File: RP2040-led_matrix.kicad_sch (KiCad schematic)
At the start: 27 parts, among them J2 USB_C_Receptacle, SW2 SW_DIP_x01, U1 W25Q16JVSS, U2 RP2040, U4 NCP1117-1.5_SOT223, Y2 ABM8-272-T3

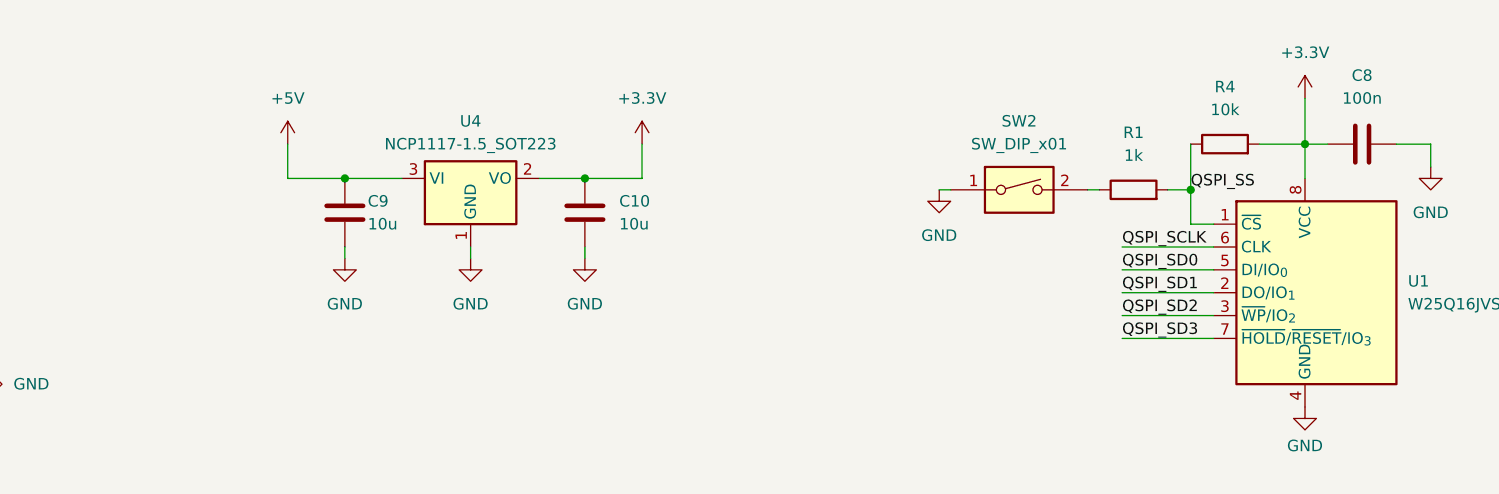
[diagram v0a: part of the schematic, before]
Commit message: Modified power supply stage
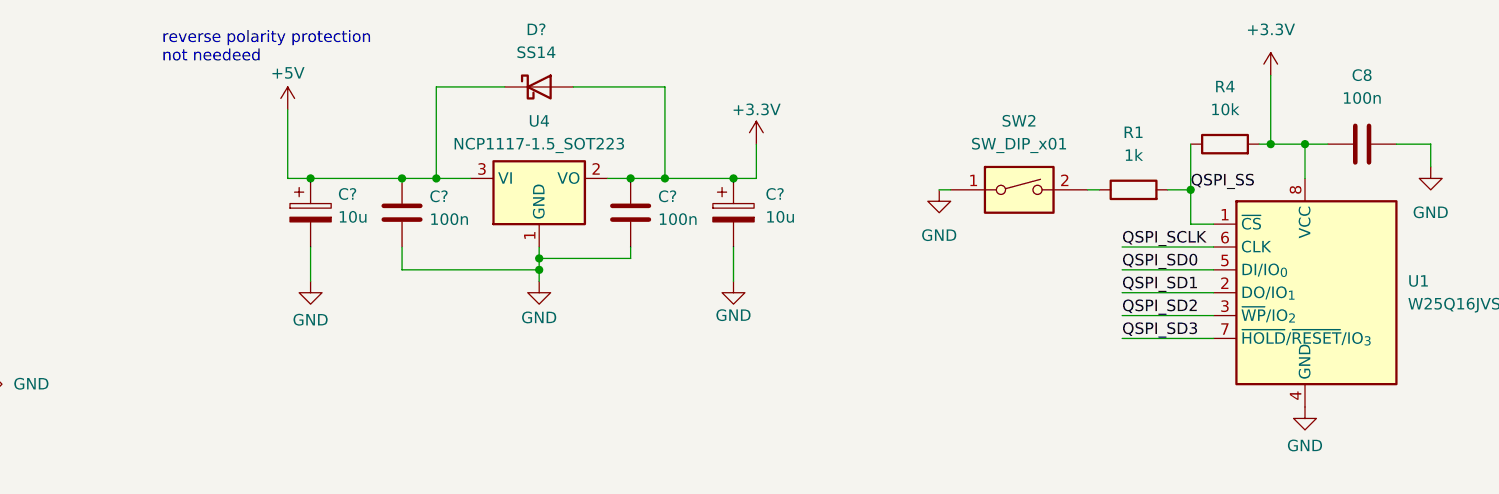
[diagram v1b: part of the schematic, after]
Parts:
- removed C10, C9: 10u, Capacitor_SMD:C_0603_1608Metric, symbol Device:C
- added C? (x2): 10u, Capacitor_SMD:CP_Elec_5x5.4, symbol Device:C_Polarized
- added C? (x2): 100n, Capacitor_SMD:C_0805_2012Metric, symbol Device:C
- added D?: SS14, Diode_THT:D_DO-41_SOD81_P10.16mm_Horizontal, symbol Diode:SS14
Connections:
- net +3.3V: now also C?.1, C?.1, D?.2 (A)
- net +5V: now also C?.1, C?.1, D?.1 (K)
- net GND: now also C?.2, C?.2, C?.2, C?.2
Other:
- note added: "reverse polarity protection not needeed"
- moved on the sheet: U4

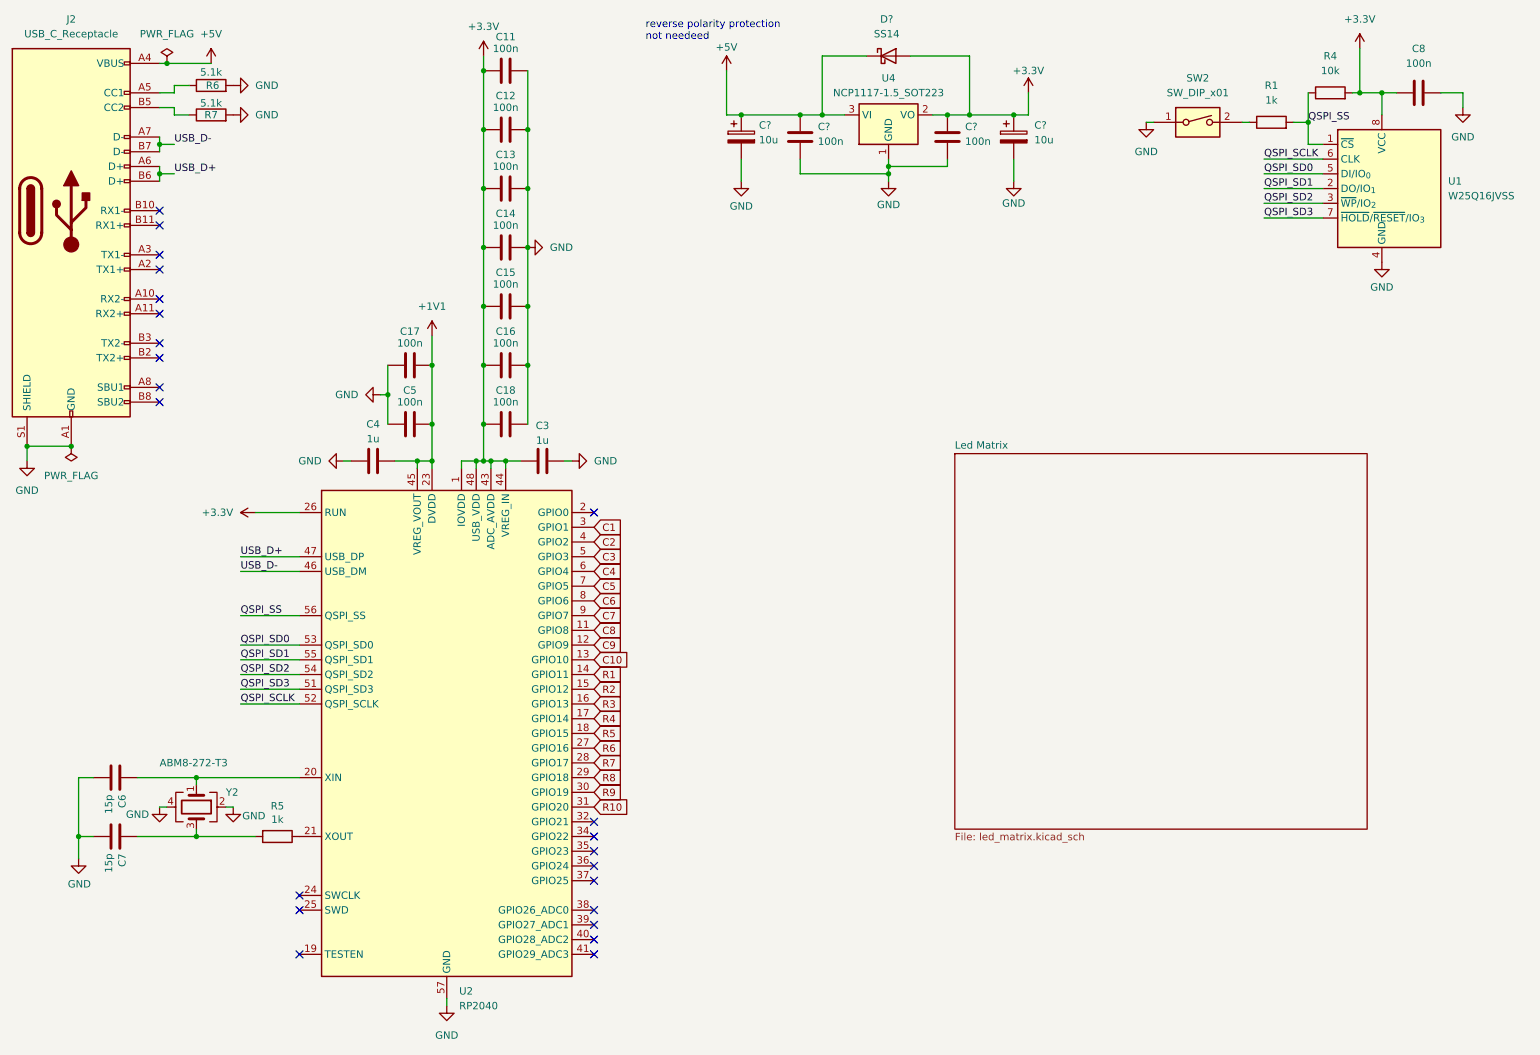
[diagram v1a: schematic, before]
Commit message: Creataed many hierarchical sheet
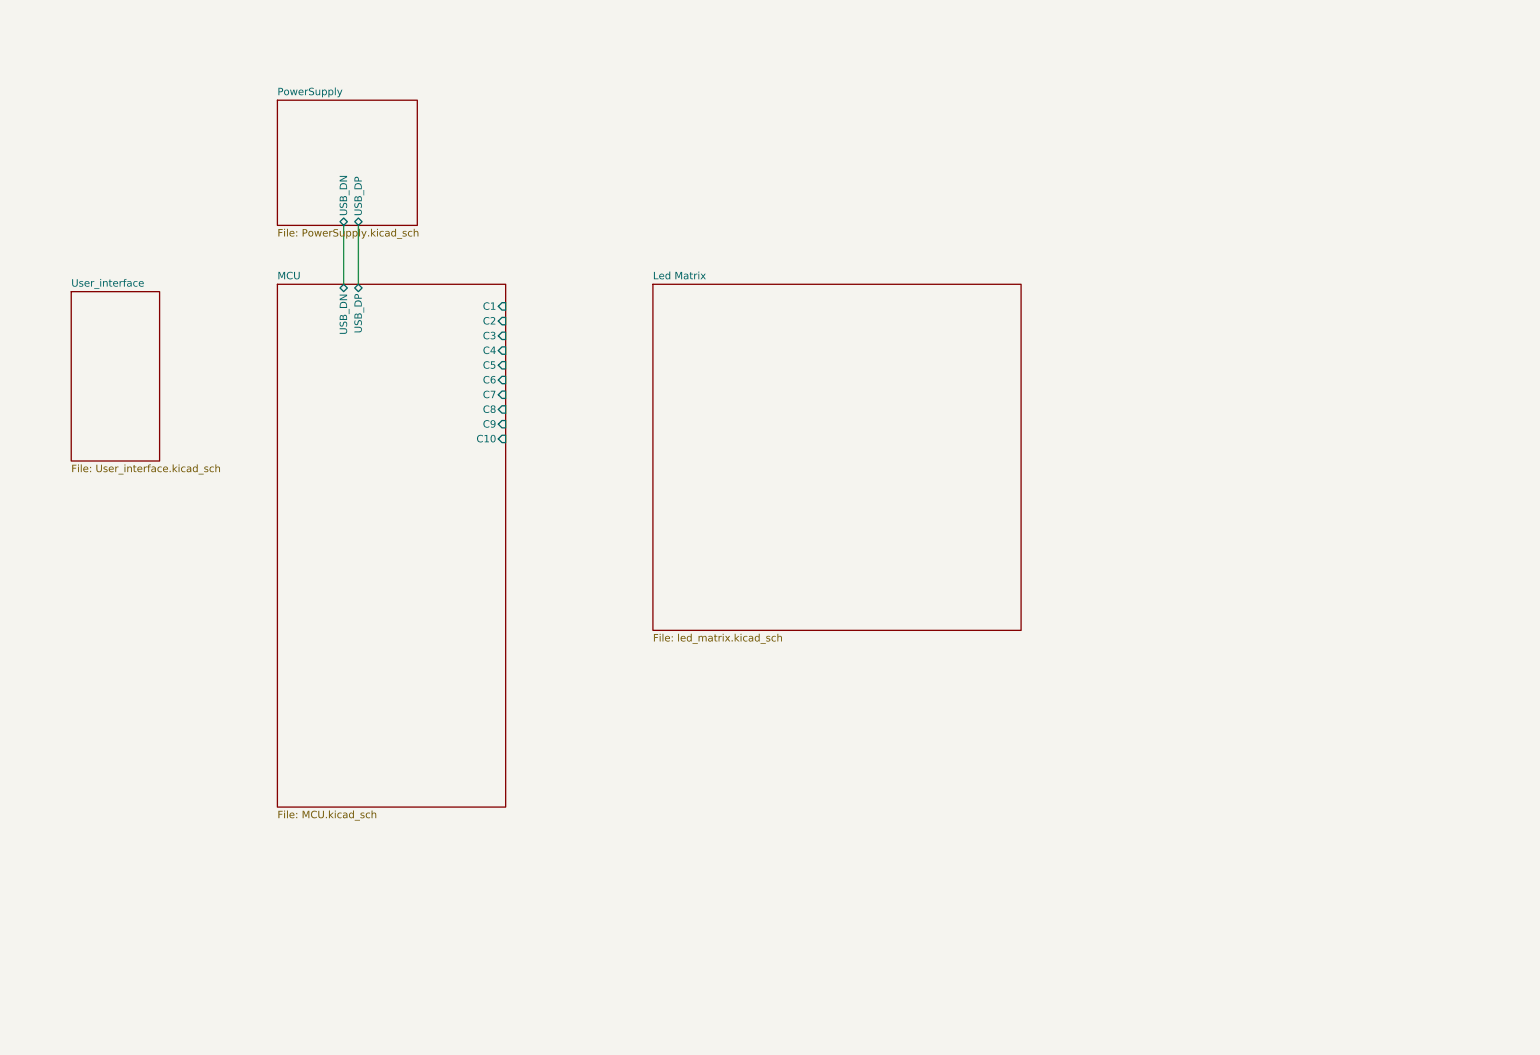
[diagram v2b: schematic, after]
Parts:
- removed C11, C12, C13, C14, C15, C16, C17, C18, C5, C8: 100n, Capacitor_SMD:C_0603_1608Metric, symbol Device:C
- removed C3, C4: 1u, Capacitor_SMD:C_0603_1608Metric, symbol Device:C
- removed C6, C7: 15p, Capacitor_SMD:C_0603_1608Metric, symbol Device:C
- removed C? (x2): 10u, Capacitor_SMD:CP_Elec_5x5.4, symbol Device:C_Polarized
- removed C? (x2): 100n, Capacitor_SMD:C_0805_2012Metric, symbol Device:C
- removed D?: SS14, Diode_THT:D_DO-41_SOD81_P10.16mm_Horizontal, symbol Diode:SS14
- removed J2: USB_C_Receptacle, Connector_USB:USB_C_Receptacle_GCT_USB4110, symbol Connector:USB_C_Receptacle
- removed R1, R5: 1k, Resistor_SMD:R_0603_1608Metric, symbol Device:R
- removed R4: 10k, Resistor_SMD:R_0603_1608Metric, symbol Device:R
- removed R6, R7: 5.1k, Resistor_SMD:R_0603_1608Metric, symbol Device:R
- removed SW2: SW_DIP_x01, Button_Switch_SMD:SW_DIP_SPSTx01_Slide_6.7x4.1mm_W6.73mm_P2.54mm_LowProfile_JPin, symbol Switch:SW_DIP_x01
- removed U1: W25Q16JVSS, Package_SO:SOIC-8_5.3x5.3mm_P1.27mm, symbol Memory_Flash:W25Q16JVSS
- removed U2: RP2040, Package_DFN_QFN:QFN-56-1EP_7x7mm_P0.4mm_EP3.2x3.2mm, symbol MCU_RaspberryPi:RP2040
- removed U4: NCP1117-1.5_SOT223, Package_TO_SOT_SMD:SOT-223-3_TabPin2, symbol Regulator_Linear:NCP1117-1.5_SOT223
- removed Y2: ABM8-272-T3, Crystal:Crystal_SMD_3225-4Pin_3.2x2.5mm, symbol Device:Crystal_GND24
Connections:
- no-connect marks 23 -> 0
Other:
- added sheet MCU (MCU.kicad_sch)
- added sheet PowerSupply (PowerSupply.kicad_sch)
- added sheet User_interface (User_interface.kicad_sch)
- note removed: "reverse polarity protection not needeed"
